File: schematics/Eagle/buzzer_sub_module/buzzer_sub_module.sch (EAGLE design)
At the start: 4 parts, among them Q1 2N3585

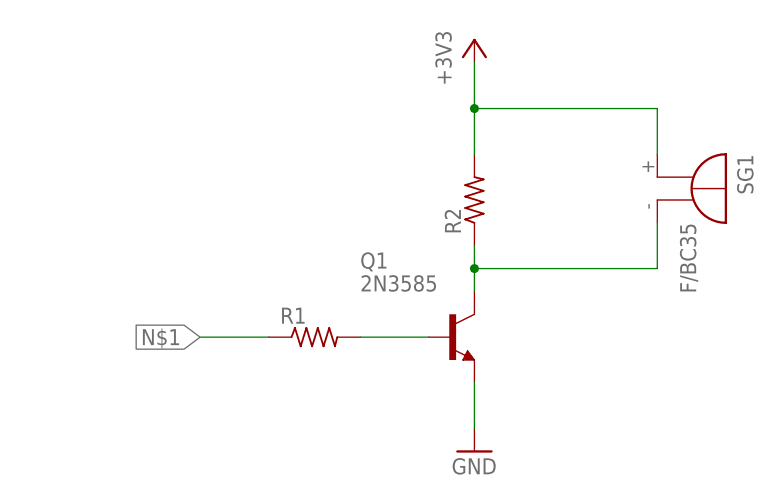
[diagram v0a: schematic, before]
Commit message: schematic fully pinned out
added psuedocode to main to test output LED's.

finished pinouts after input from team's sub-module requests.
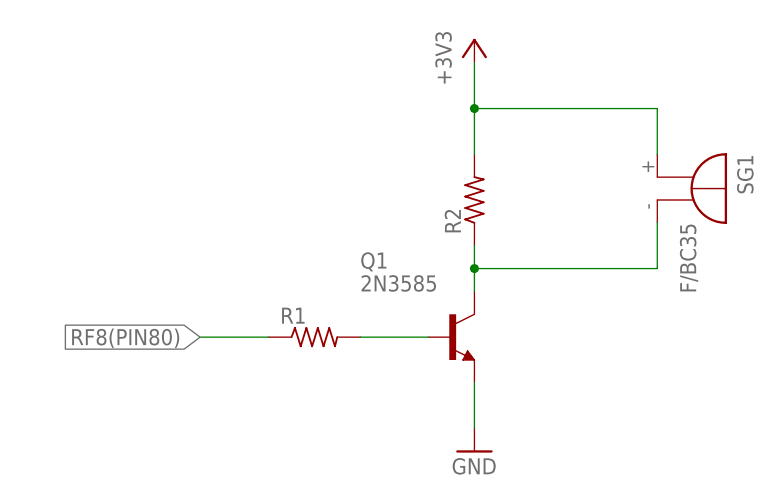
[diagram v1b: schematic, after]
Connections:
- net N$1 renamed RF8(PIN80)
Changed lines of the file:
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@@
 <setting verticaltext="up"/>
 </settings>
-<grid distance="0.1" unitdist="inch" unit="inch" style="lines" multiple="1" display="yes" altdistance="0.01" altunitdist="inch" altunit="inch"/>
+<grid distance="0.1" unitdist="inch" unit="inch" style="lines" multiple="1" display="no" altdistance="0.01" altunitdist="inch" altunit="inch"/>
 <layers>
 <layer number="1" name="Top" color="4" fill="1" visible="no" active="no"/>
@@
 </busses>
 <nets>
-<net name="N$1" class="0">
+<net name="RF8(PIN80)" class="0">
 <segment>
 <pinref part="R1" gate="G$1" pin="1"/>

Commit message: adjusted a schematic and added a datasheet
scheamtic updated with values for buzzer.

also uploading a worksheet that chad and I did for the motors and buzzer
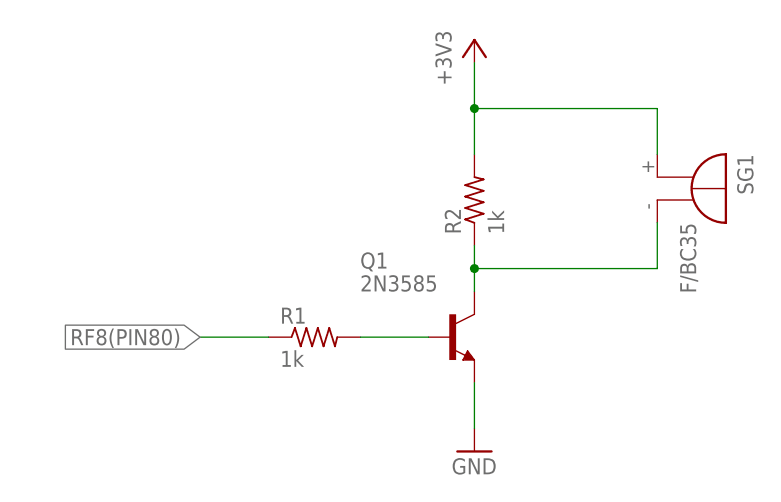
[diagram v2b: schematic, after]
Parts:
- R1, R2: value (none) -> 1k
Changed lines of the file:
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@@
 <part name="SG1" library="buzzer" deviceset="F/BC35" device=""/>
 <part name="GND2" library="supply1" deviceset="GND" device=""/>
-<part name="R1" library="resistor" deviceset="R-US_" device="0204/2V"/>
-<part name="R2" library="resistor" deviceset="R-US_" device="0204/2V"/>
+<part name="R1" library="resistor" deviceset="R-US_" device="0204/2V" value="1k"/>
+<part name="R2" library="resistor" deviceset="R-US_" device="0204/2V" value="1k"/>
 <part name="+3V1" library="supply1" deviceset="+3V3" device=""/>
 </parts>
